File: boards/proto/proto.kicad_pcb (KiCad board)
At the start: 2 copper layers, 100 x 100 mm, 5 parts, among them J1 XBUS_02, J2 PIA_INT, J3 VIA_INT, J4 ACIA_INT

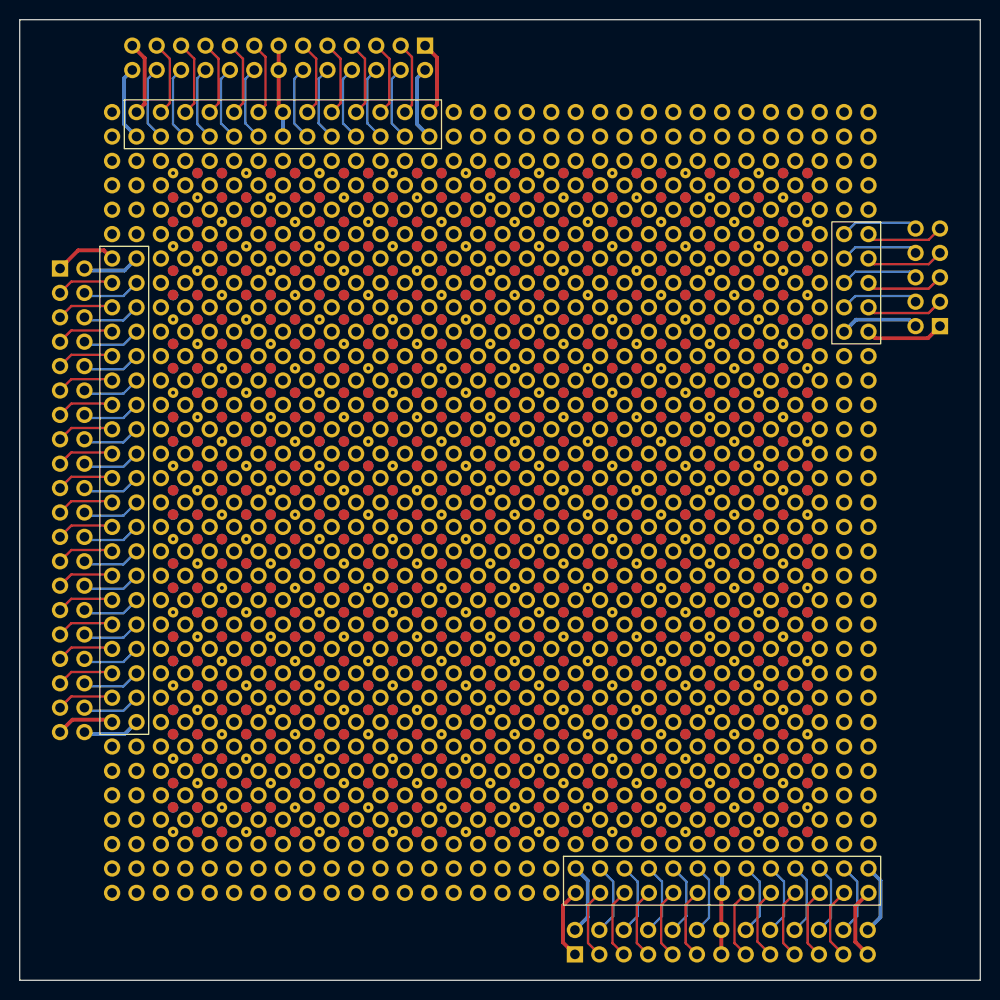
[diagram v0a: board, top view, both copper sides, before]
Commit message: Connect power traces across prototype board.
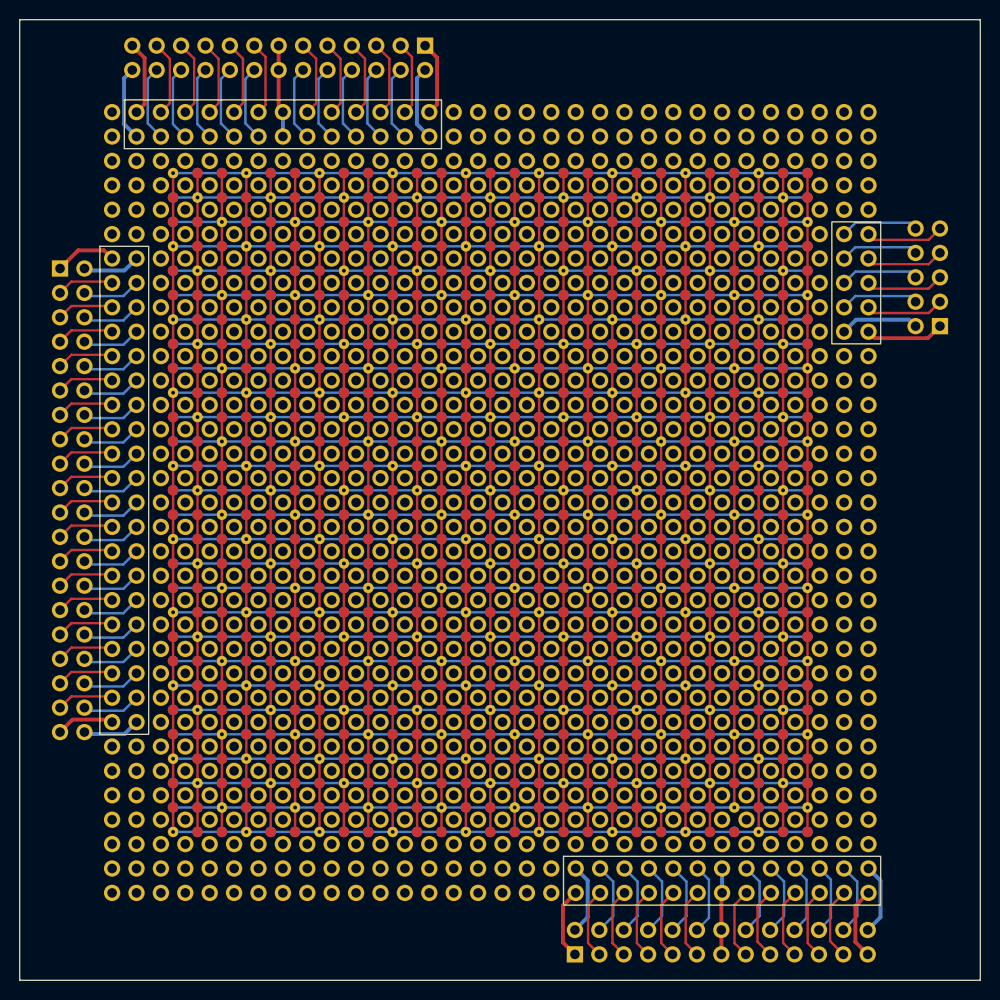
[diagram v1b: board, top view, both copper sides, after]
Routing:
- net (no net): track 0.00 -> 3698.2 mm

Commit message: Power traces were bad/disconnected. Incrementally redo them/add scripting.
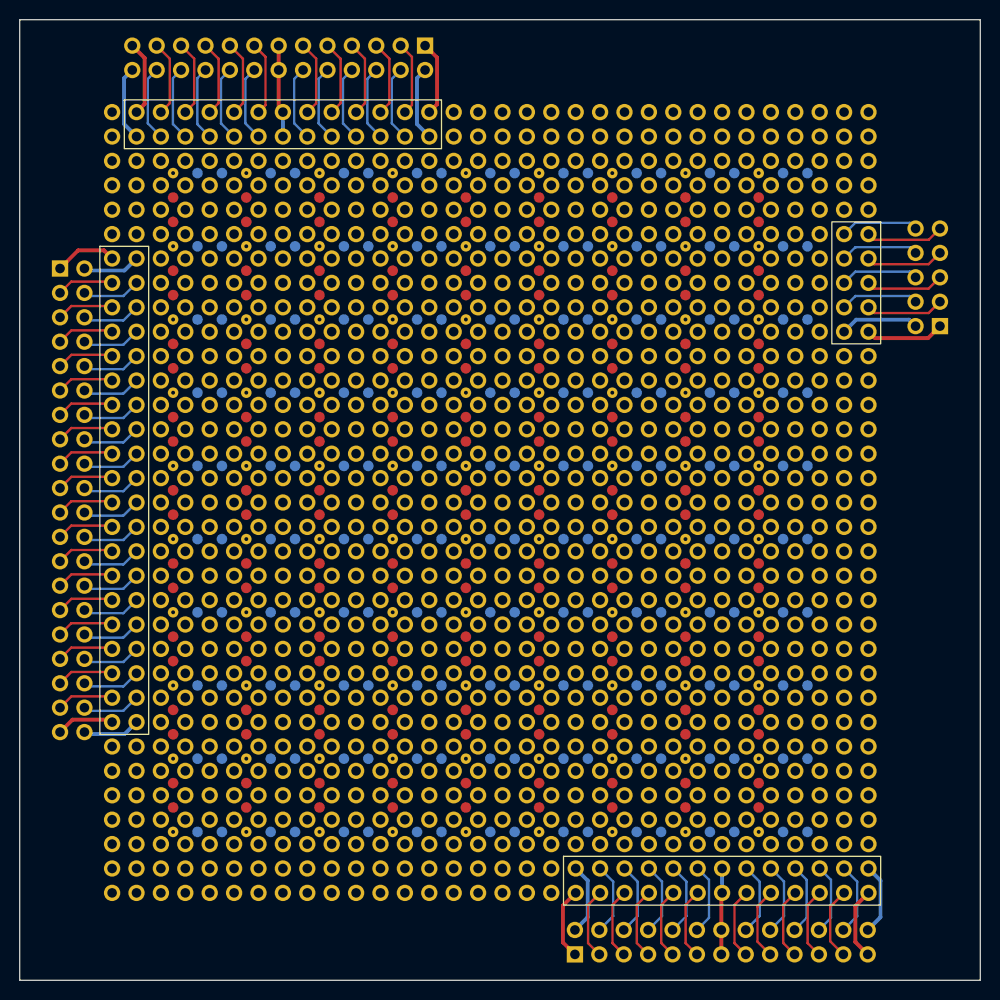
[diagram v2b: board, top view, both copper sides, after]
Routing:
- net (no net): track 3698.2 -> 0.00 mm
